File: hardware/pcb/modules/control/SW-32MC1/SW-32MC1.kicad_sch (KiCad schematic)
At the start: 60 parts, among them J1 JTAG, J2 ESPFlash, J3 FP_5V, J4 FP_IO, J5 OLED, J6 RESET/FLASH, J7 I2C, Q1 Q_NMOS_DGS, SW1 PEC11R-4225F-50024, SW2 DNP, SW3 DNP, U1 ESP32-WROOM-32D

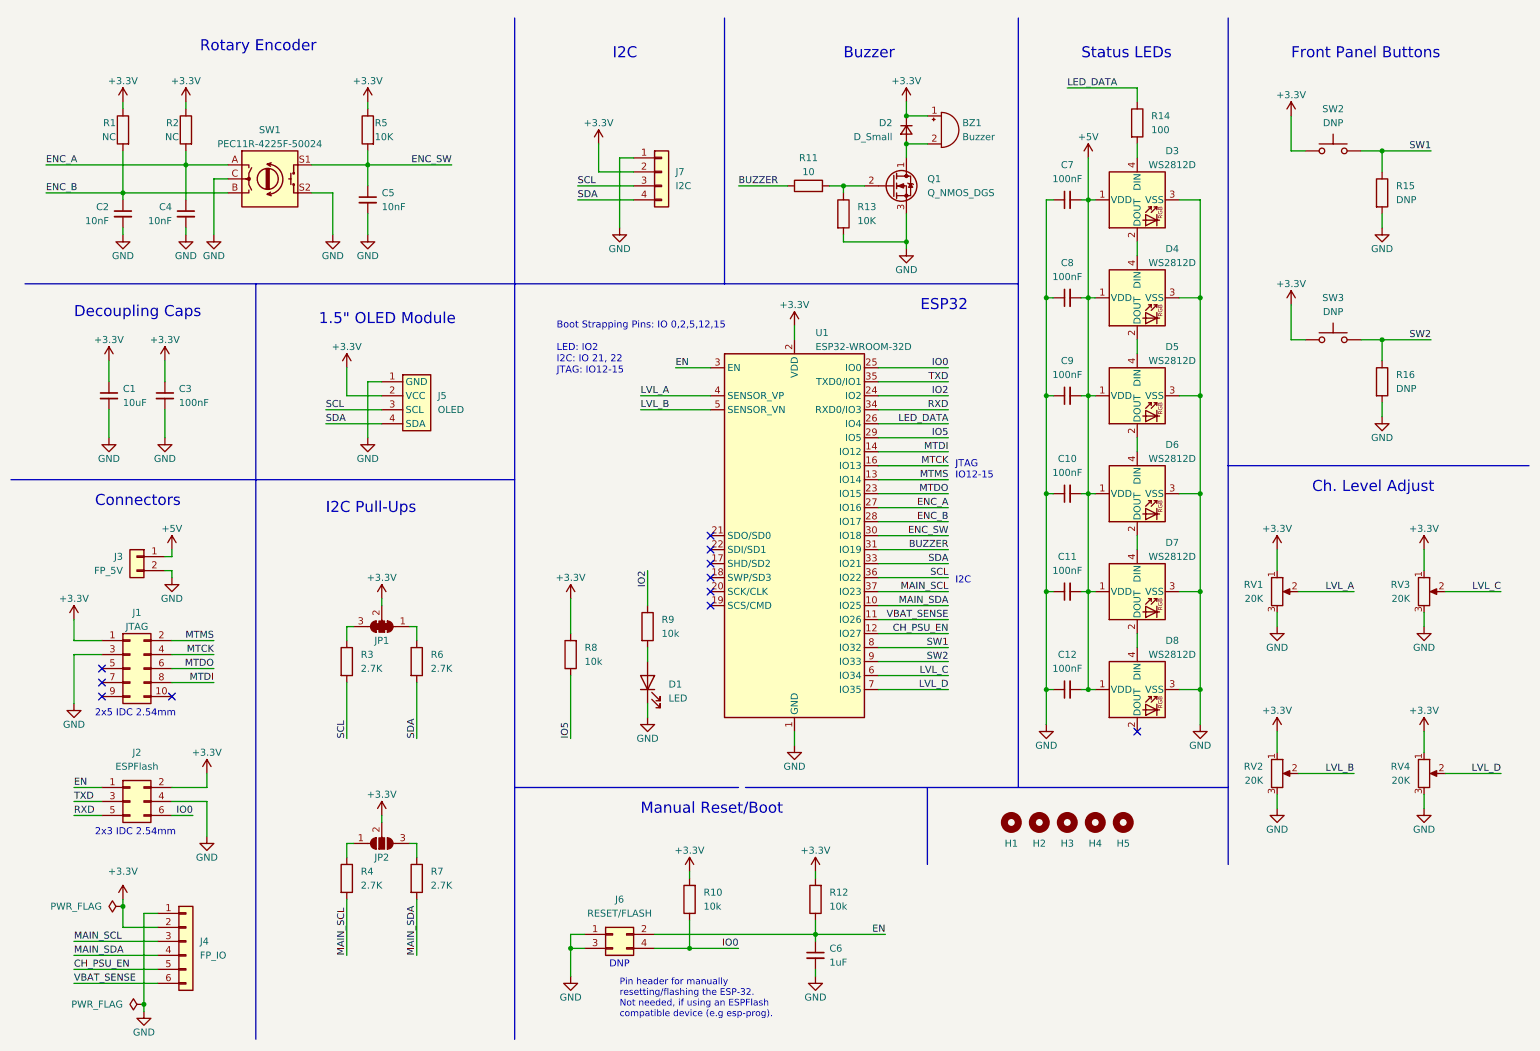
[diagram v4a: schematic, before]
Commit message: use 5v for front panel connector
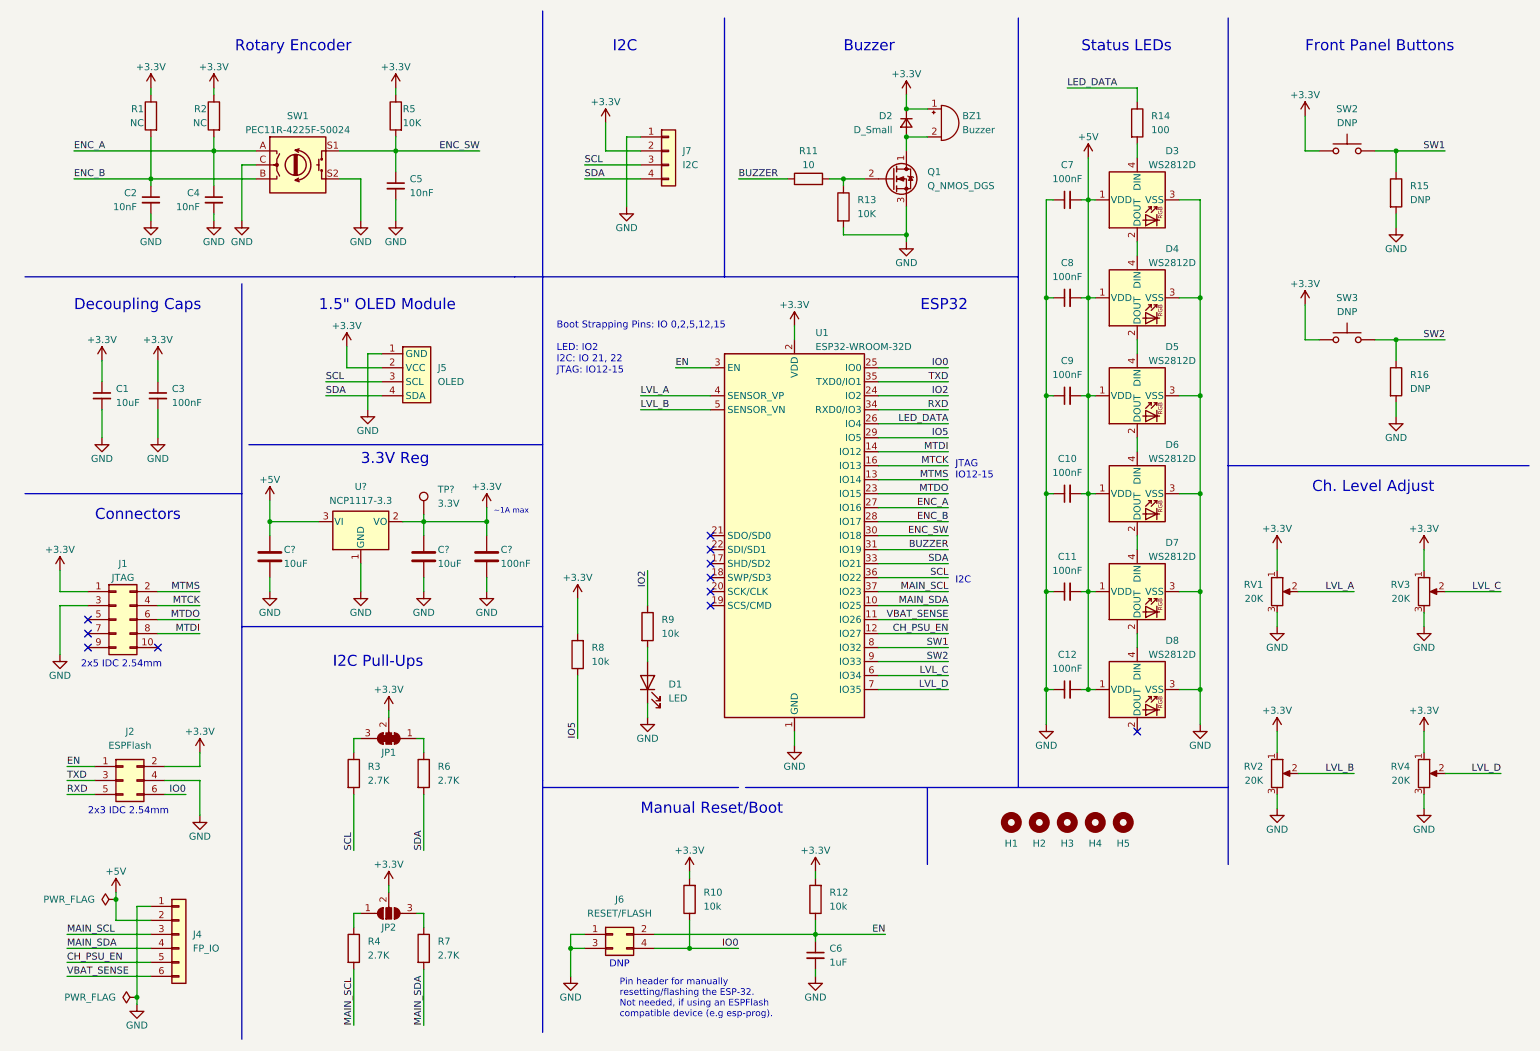
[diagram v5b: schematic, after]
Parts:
- removed J3: FP_5V, Connector_JST:JST_XH_B2B-XH-A_1x02_P2.50mm_Vertical, symbol Connector_Generic:Conn_01x02
- added C? (x2): 10uF, Capacitor_SMD:C_0603_1608Metric, symbol Device:C
- added C?: 100nF, Capacitor_SMD:C_0603_1608Metric, symbol Device:C
- added TP?: 3.3V, TestPoint:TestPoint_THTPad_D2.0mm_Drill1.0mm, symbol Connector:TestPoint
- added U?: NCP1117-3.3, Package_TO_SOT_SMD:SOT-223-3_TabPin2, symbol Regulator_Linear:NCP1117-3.3_SOT223
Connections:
- net +3V3: now also C?.1, C?.1, TP?.1, U?.2 (VO); no longer J4.2 (Pin_2)
- net +5V: now also J4.2 (Pin_2), C?.1, U?.3 (VI)
- net GND: now also C?.2, C?.2, C?.2, U?.1 (GND)
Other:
- note added: "3.3V Reg"
- note added: "~1A max"
- moved on the sheet: BZ1, C1, C2, C3, C4, C5, D2, J1, J2, J4, J5, J7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

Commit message: major changes
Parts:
- removed C6: 1uF, Capacitor_SMD:C_0603_1608Metric, symbol Device:C_Small
- removed C? (x2): 10uF, Capacitor_SMD:C_0603_1608Metric, symbol Device:C
- removed C?: 100nF, Capacitor_SMD:C_0603_1608Metric, symbol Device:C
- removed J6: RESET/FLASH, Connector_PinHeader_2.54mm:PinHeader_2x02_P2.54mm_Vertical, symbol Connector_Generic:Conn_02x02_Odd_Even
- removed JP2: SolderJumper_3_Open, symbol Jumper:SolderJumper_3_Open
- removed R10, R12: 10k, Resistor_SMD:R_0603_1608Metric, symbol Device:R
- removed R14: 100, symbol Device:R
- removed R16: DNP, Resistor_SMD:R_0603_1608Metric, symbol Device:R
- removed R4, R7: 2.7K, Resistor_SMD:R_0603_1608Metric, symbol Device:R
- removed SW3: DNP, Button_Switch_SMD:SW_Push_1P1T_NO_6x6mm_H9.5mm, symbol Switch:SW_Push
- removed TP?: 3.3V, TestPoint:TestPoint_THTPad_D2.0mm_Drill1.0mm, symbol Connector:TestPoint
- removed U?: NCP1117-3.3, Package_TO_SOT_SMD:SOT-223-3_TabPin2, symbol Regulator_Linear:NCP1117-3.3_SOT223
- added D3: D, Diode_SMD:D_SOD-123F, symbol Device:D
- added D4: WS2812D, SaawLib:WS2812D-F5, symbol SaawLib:WS2812D
- added JP1, JP2: SolderJumper_3_Bridged12, Jumper:SolderJumper-3_P1.3mm_Bridged12_Pad1.0x1.5mm_NumberLabels, symbol Jumper:SolderJumper_3_Bridged12
- BZ1: footprint (none) -> Buzzer_Beeper:Buzzer_12x9.5RM7.6
- C10: renamed from C11; footprint (none) -> Capacitor_SMD:C_0603_1608Metric
- C11: renamed from C12; footprint (none) -> Capacitor_SMD:C_0603_1608Metric
- C6: renamed from C7; footprint (none) -> Capacitor_SMD:C_0603_1608Metric
- C7: renamed from C8; footprint (none) -> Capacitor_SMD:C_0603_1608Metric
- C8: renamed from C9; footprint (none) -> Capacitor_SMD:C_0603_1608Metric
- C9: renamed from C10; footprint (none) -> Capacitor_SMD:C_0603_1608Metric
- D1: footprint (none) -> LED_SMD:LED_0603_1608Metric
- D10: renamed from D8; footprint (none) -> SaawLib:WS2812D-F5; symbol LED:WS2812B -> SaawLib:WS2812D; LCSC (none) -> C190565; MPN (none) -> WS2812D-F5
- D2: footprint (none) -> Diode_SMD:D_SOD-123F
- D5: renamed from D3; footprint (none) -> SaawLib:WS2812D-F5; symbol LED:WS2812B -> SaawLib:WS2812D; LCSC (none) -> C190565; MPN (none) -> WS2812D-F5
- D6: renamed from D4; footprint (none) -> SaawLib:WS2812D-F5; symbol LED:WS2812B -> SaawLib:WS2812D; LCSC (none) -> C190565; MPN (none) -> WS2812D-F5
- D7: renamed from D5; footprint (none) -> SaawLib:WS2812D-F5; symbol LED:WS2812B -> SaawLib:WS2812D; LCSC (none) -> C190565; MPN (none) -> WS2812D-F5
- D8: renamed from D6; footprint (none) -> SaawLib:WS2812D-F5; symbol LED:WS2812B -> SaawLib:WS2812D; LCSC (none) -> C190565; MPN (none) -> WS2812D-F5
- D9: renamed from D7; footprint (none) -> SaawLib:WS2812D-F5; symbol LED:WS2812B -> SaawLib:WS2812D; LCSC (none) -> C190565; MPN (none) -> WS2812D-F5
- H1, H2, H3, H4, H5: now left out of the parts list
- J1: footprint Connector_PinHeader_2.54mm:PinHeader_2x05_P2.54mm_Vertical -> Connector_IDC:IDC-Header_2x05_P2.54mm_Vertical
- J2: footprint Connector_PinHeader_2.54mm:PinHeader_2x03_P2.54mm_Vertical -> Connector_IDC:IDC-Header_2x03_P2.54mm_Vertical
- J3: renamed from J5; footprint SaawLib:OLED_I2C -> SaawLib:OLED_I2C_1.3
- J4: footprint (none) -> Connector_JST:JST_XH_B8B-XH-A_1x08_P2.50mm_Vertical; symbol Connector_Generic:Conn_01x06 -> Connector_Generic:Conn_01x08
- J5: renamed from J7; footprint (none) -> Connector_PinHeader_2.54mm:PinHeader_1x04_P2.54mm_Vertical
- Q1: value Q_NMOS_DGS -> DMN2040U; footprint (none) -> Package_TO_SOT_SMD:SOT-23; symbol Device:Q_NMOS_DGS -> Device:Q_NMOS_SGD
- R1, R2: value NC -> 10K; now in the parts list
- R10: renamed from R15; value DNP -> 10K
- R8: renamed from R11; footprint (none) -> Resistor_SMD:R_0603_1608Metric
- R9: renamed from R13; footprint (none) -> Resistor_SMD:R_0603_1608Metric
- SW1: value PEC11R-4225F-50024 -> PEC11R-4225F-S0024
- U1: MPN (none) -> ESP32-WROOM-32D
- renumbered C2 to C1, C4 to C2, C1 to C3, C3 to C4, JP1 to JP3, R8 to R3, R5 to R4, R9 to R5, R3 to R6, R6 to R7
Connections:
- net +3V3: now also J4.3 (Pin_3), JP1.1 (A), JP2.3 (B); no longer J3.2 (VCC)
- net +5V: now also D10.2 (VCC), D5.2 (VCC), D6.2 (VCC), D7.2 (VCC), D8.2 (VCC), D9.2 (VCC), D3.2 (A); no longer D10.1 (VDD), D5.1 (VDD), D6.1 (VDD), D7.1 (VDD), D8.1 (VDD), D9.1 (VDD)
- net GND: now also Q1.1 (S), D4.3 (GND), JP1.3 (B), JP2.1 (A); no longer J3.1 (GND), Q1.3 (S)
- net LED_DATA: now also D4.4 (DIN)
- net MAIN_SCL: now also J4.4 (Pin_4); no longer J4.3 (Pin_3)
- net MAIN_SDA: now also J4.5 (Pin_5); no longer J4.4 (Pin_4)
- net at D5.4 (DIN): now also D4.1 (DOUT)
- net at D10.4 (DIN): now also D9.1 (DOUT); no longer D9.2 (DOUT)
- net at D9.4 (DIN): now also D8.1 (DOUT); no longer D8.2 (DOUT)
- net at BZ1.2 (+), D2.2 (A): now also Q1.3 (D); no longer Q1.1 (D)
- net at D8.4 (DIN): now also D7.1 (DOUT); no longer D7.2 (DOUT)
- net at D7.4 (DIN): now also D6.1 (DOUT); no longer D6.2 (DOUT)
- net at D6.4 (DIN): now also D5.1 (DOUT); no longer D5.2 (DOUT)
- net CH_PSU_EN renamed LINE_LEFT
- net LINE_LEFT: now also J4.7 (Pin_7); no longer J4.5 (Pin_5)
- net SW2 renamed LINE_RIGHT
- net LINE_RIGHT: now also J4.6 (Pin_6)
- net VBAT_SENSE renamed MIC
- net MIC: now also J4.8 (Pin_8); no longer J4.6 (Pin_6)
- new net: J3.1 (GND), JP2.2 (C)
- new net: J3.2 (VCC), JP1.2 (C)
- new net: D3.1 (K), D4.2 (VCC)
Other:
- note added: "Back/Multi Button"
- note added: "First LED acts as level shifter & is hidden"
- note added: "~0.7V"
- note removed: "2x3 IDC 2.54mm"
- note removed: "2x5 IDC 2.54mm"
- note removed: "3.3V Reg"
- note removed: "DNP"
- note removed: "Decoupling Caps"
- note removed: "Front Panel Buttons"
- note removed: "Manual Reset/Boot"
- note removed: "Pin header for manually resetting/flashing the ESP-32. Not needed, if using an ESPFlash compatible device (e.g esp-prog)."
- note removed: "~1A max"
- moved on the sheet: C10, C11, C3, C4, C6, C7, C8, C9, D1, J3, JP3, R10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
